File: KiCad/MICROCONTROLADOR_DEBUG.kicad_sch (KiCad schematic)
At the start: 9 parts, among them U7 PIC24HJ128GP504-I_PT, Y1 8MHz

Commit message: Inputs
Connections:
- net DOOR_BTN_CLOSED: no longer names the net of U7.32 (TDO/PMA8/RA8)
- net DOOR_BTN_OPEN: no longer names the net of U7.13 (TCK/PMA7/RA7)
- net DOOR_LOCK_SW: no longer names the net of U7.35 (TDI/PMA9/RA9)
- net DOOR_UNLOCK_SW renamed DOOR_LOCK/UNLOCK
- no-connect marks 2 -> 5
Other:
- moved on the sheet: C_OSC1, C_OSC2, Y1
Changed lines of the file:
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@@
 	)
 	(junction
-		(at 64.77 74.93)
+		(at 60.96 74.93)
 		(diameter 0)
 		(color 0 0 0 0)
@@
 	)
 	(junction
-		(at 48.26 74.93)
+		(at 44.45 74.93)
 		(diameter 0)
 		(color 0 0 0 0)
@@
 	)
 	(no_connect
+		(at 93.98 71.12)
+	)
+	(no_connect
 		(at 93.98 60.96)
+	)
+	(no_connect
+		(at 93.98 73.66)
+	)
+	(no_connect
+		(at 93.98 76.2)
 	)
 	(no_connect
@@
 	(wire
 		(pts
-			(xy 48.26 74.93) (xy 53.34 74.93)
+			(xy 44.45 74.93) (xy 49.53 74.93)
 		)
 		(stroke
@@
 	(wire
 		(pts
-			(xy 64.77 74.93) (xy 64.77 77.47)
+			(xy 60.96 74.93) (xy 60.96 77.47)
 		)
 		(stroke
@@
 	(wire
 		(pts
-			(xy 60.96 74.93) (xy 64.77 74.93)
+			(xy 57.15 74.93) (xy 60.96 74.93)
 		)
 		(stroke
@@
 	(wire
 		(pts
-			(xy 48.26 74.93) (xy 48.26 77.47)
+			(xy 44.45 74.93) (xy 44.45 77.47)
 		)
 		(stroke
@@
 	(wire
 		(pts
-			(xy 48.26 63.5) (xy 48.26 74.93)
+			(xy 44.45 63.5) (xy 44.45 74.93)
 		)
 		(stroke
@@
 	(wire
 		(pts
-			(xy 64.77 66.04) (xy 64.77 74.93)
+			(xy 60.96 66.04) (xy 60.96 74.93)
 		)
 		(stroke
@@
 	(wire
 		(pts
-			(xy 93.98 66.04) (xy 64.77 66.04)
-		)
-		(stroke
-			(width 0)
-			(type default)
-		)
-	)
-	(wire
-		(pts
-			(xy 93.98 63.5) (xy 48.26 63.5)
+			(xy 60.96 66.04) (xy 93.98 66.04)
+		)
+		(stroke
+			(width 0)
+			(type default)
+		)
+	)
+	(wire
+		(pts
+			(xy 44.45 63.5) (xy 93.98 63.5)
 		)
 		(stroke
@@
 		)
 	)
-	(hierarchical_label "DOOR_BTN_OPEN"
-		(shape input)
-		(at 93.98 71.12 180)
-		(effects
-			(font
-				(size 1.27 1.27)
-			)
-			(justify right)
-		)
-	)
 	(hierarchical_label "RFID_CS"
 		(shape output)
@@
 		)
 	)
-	(hierarchical_label "DOOR_BTN_CLOSED"
-		(shape input)
-		(at 93.98 73.66 180)
-		(effects
-			(font
-				(size 1.27 1.27)
-			)
-			(justify right)
-		)
-	)
 	(hierarchical_label "DOOR_LIMIT_CLOSE"
 		(shape input)
@@
 		)
 	)
-	(hierarchical_label "DOOR_LOCK_SW"
-		(shape input)
-		(at 93.98 76.2 180)
-		(effects
-			(font
-				(size 1.27 1.27)
-			)
-			(justify right)
-		)
-	)
 	(hierarchical_label "WIN_PWM"
 		(shape output)
@@
 		)
 	)
-	(hierarchical_label "DOOR_UNLOCK_SW"
+	(hierarchical_label "DOOR_LOCK{slash}UNLOCK"
 		(shape input)
 		(at 93.98 78.74 180)
@@
 	(symbol
 		(lib_id "Device:C")
-		(at 64.77 81.28 0)
+		(at 60.96 81.28 0)
 		(unit 1)
 		(exclude_from_sim no)
@@
 		(fields_autoplaced yes)
 		(property "Reference" "C_OSC2"
-			(at 68.58 80.0099 0)
+			(at 64.77 80.0099 0)
 			(effects
 				(font
@@
 		)
 		(property "Value" "22pF"
-			(at 68.58 82.5499 0)
+			(at 64.77 82.5499 0)
 			(effects
 				(font
@@
 		)
 		(property "Footprint" "Capacitor_SMD:C_0603_1608Metric"
-			(at 65.7352 85.09 0)
+			(at 61.9252 85.09 0)
 			(effects
 				(font
@@
 		)
 		(property "Datasheet" "~"
-			(at 64.77 81.28 0)
+			(at 60.96 81.28 0)
 			(effects
 				(font
@@
 		)
 		(property "Description" "Unpolarized capacitor"
-			(at 64.77 81.28 0)
+			(at 60.96 81.28 0)
 			(effects
 				(font
@@
 	(symbol
 		(lib_id "Device:Crystal")
-		(at 57.15 74.93 0)
+		(at 53.34 74.93 0)
 		(unit 1)
 		(exclude_from_sim no)
@@
 		(fields_autoplaced yes)
 		(property "Reference" "Y1"
-			(at 57.15 67.31 0)
+			(at 53.34 67.31 0)
 			(effects
 				(font
@@
 		)
 		(property "Value" "8MHz"
-			(at 57.15 69.85 0)
+			(at 53.34 69.85 0)
 			(effects
 				(font
@@
 		)
 		(property "Footprint" "Crystal:Crystal_SMD_3225-4Pin_3.2x2.5mm"
-			(at 57.15 74.93 0)
+			(at 53.34 74.93 0)
 			(effects
 				(font
@@
 		)
 		(property "Datasheet" "~"
-			(at 57.15 74.93 0)
+			(at 53.34 74.93 0)
 			(effects
 				(font
@@
 		)
 		(property "Description" "Two pin crystal"
-			(at 57.15 74.93 0)
+			(at 53.34 74.93 0)
 			(effects
 				(font
@@
 	(symbol
 		(lib_id "power:GND")
-		(at 48.26 85.09 0)
+		(at 44.45 85.09 0)
 		(unit 1)
 		(exclude_from_sim no)
@@
 		(fields_autoplaced yes)
 		(property "Reference" "#PWR09"
-			(at 48.26 91.44 0)
+			(at 44.45 91.44 0)
 			(effects
 				(font
@@
 		)
 		(property "Value" "GND"
-			(at 48.26 90.17 0)
+			(at 44.45 90.17 0)
 			(effects
 				(font
@@
 		)
 		(property "Footprint" ""
-			(at 48.26 85.09 0)
+			(at 44.45 85.09 0)
 			(effects
 				(font
@@
 		)
 		(property "Datasheet" ""
-			(at 48.26 85.09 0)
+			(at 44.45 85.09 0)
 			(effects
 				(font
@@
 		)
 		(property "Description" "Power symbol creates a global label with name \"GND\" , ground"
-			(at 48.26 85.09 0)
+			(at 44.45 85.09 0)
 			(effects
 				(font
@@
 	(symbol
 		(lib_id "power:GND")
-		(at 64.77 85.09 0)
+		(at 60.96 85.09 0)
 		(unit 1)
 		(exclude_from_sim no)
@@
 		(fields_autoplaced yes)
 		(property "Reference" "#PWR010"
-			(at 64.77 91.44 0)
+			(at 60.96 91.44 0)
 			(effects
 				(font
@@
 		)
 		(property "Value" "GND"
-			(at 64.77 90.17 0)
+			(at 60.96 90.17 0)
 			(effects
 				(font
@@
 		)
 		(property "Footprint" ""
-			(at 64.77 85.09 0)
+			(at 60.96 85.09 0)
 			(effects
 				(font
@@
 		)
 		(property "Datasheet" ""
-			(at 64.77 85.09 0)
+			(at 60.96 85.09 0)
 			(effects
 				(font
@@
 		)
 		(property "Description" "Power symbol creates a global label with name \"GND\" , ground"
-			(at 64.77 85.09 0)
+			(at 60.96 85.09 0)
 			(effects
 				(font
@@
 	(symbol
 		(lib_id "Device:C")
-		(at 48.26 81.28 0)
+		(at 44.45 81.28 0)
 		(unit 1)
 		(exclude_from_sim no)
@@
 		(fields_autoplaced yes)
 		(property "Reference" "C_OSC1"
-			(at 52.07 80.0099 0)
+			(at 48.26 80.0099 0)
 			(effects
 				(font
@@
 		)
 		(property "Value" "22pF"
-			(at 52.07 82.5499 0)
+			(at 48.26 82.5499 0)
 			(effects
 				(font
@@
 		)
 		(property "Footprint" "Capacitor_SMD:C_0603_1608Metric"
-			(at 49.2252 85.09 0)
+			(at 45.4152 85.09 0)
 			(effects
 				(font
@@
 		)
 		(property "Datasheet" "~"
-			(at 48.26 81.28 0)
+			(at 44.45 81.28 0)
 			(effects
 				(font
@@
 		)
 		(property "Description" "Unpolarized capacitor"
-			(at 48.26 81.28 0)
-			(effects
-				(font
+			(at 44.45 81.28 0)
+			(effects
+				(font

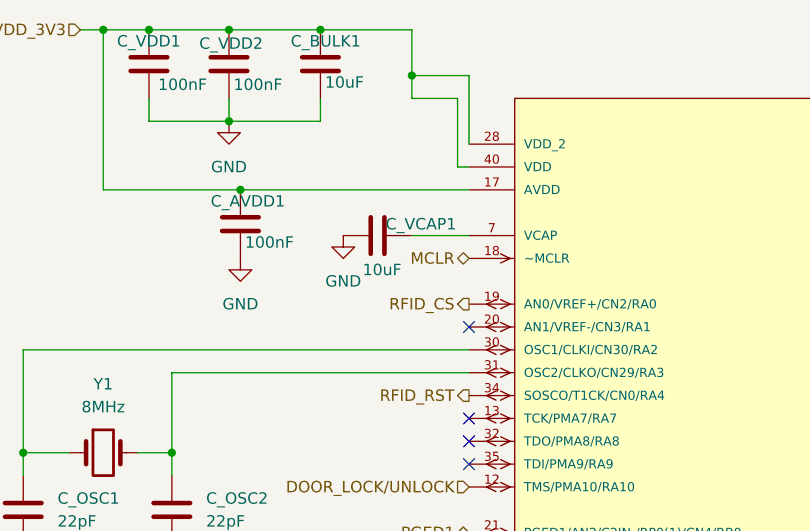
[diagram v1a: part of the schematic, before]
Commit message: Bus CAN i USART
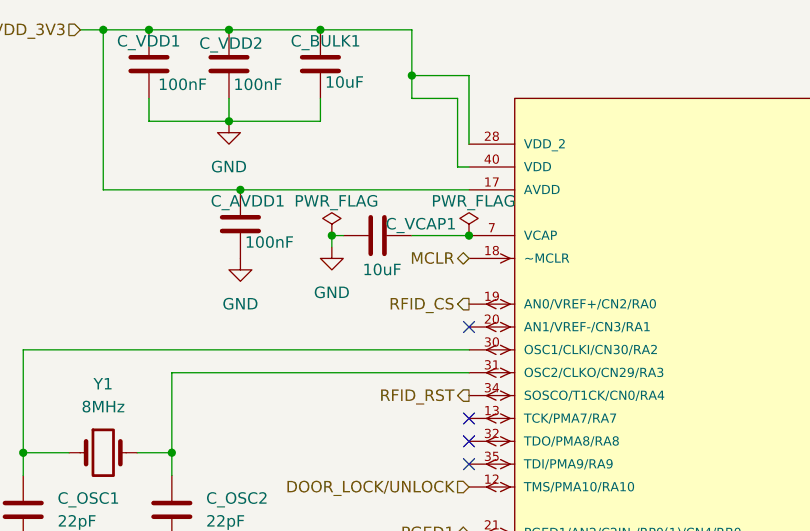
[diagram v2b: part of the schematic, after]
